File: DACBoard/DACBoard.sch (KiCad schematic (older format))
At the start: 71 parts

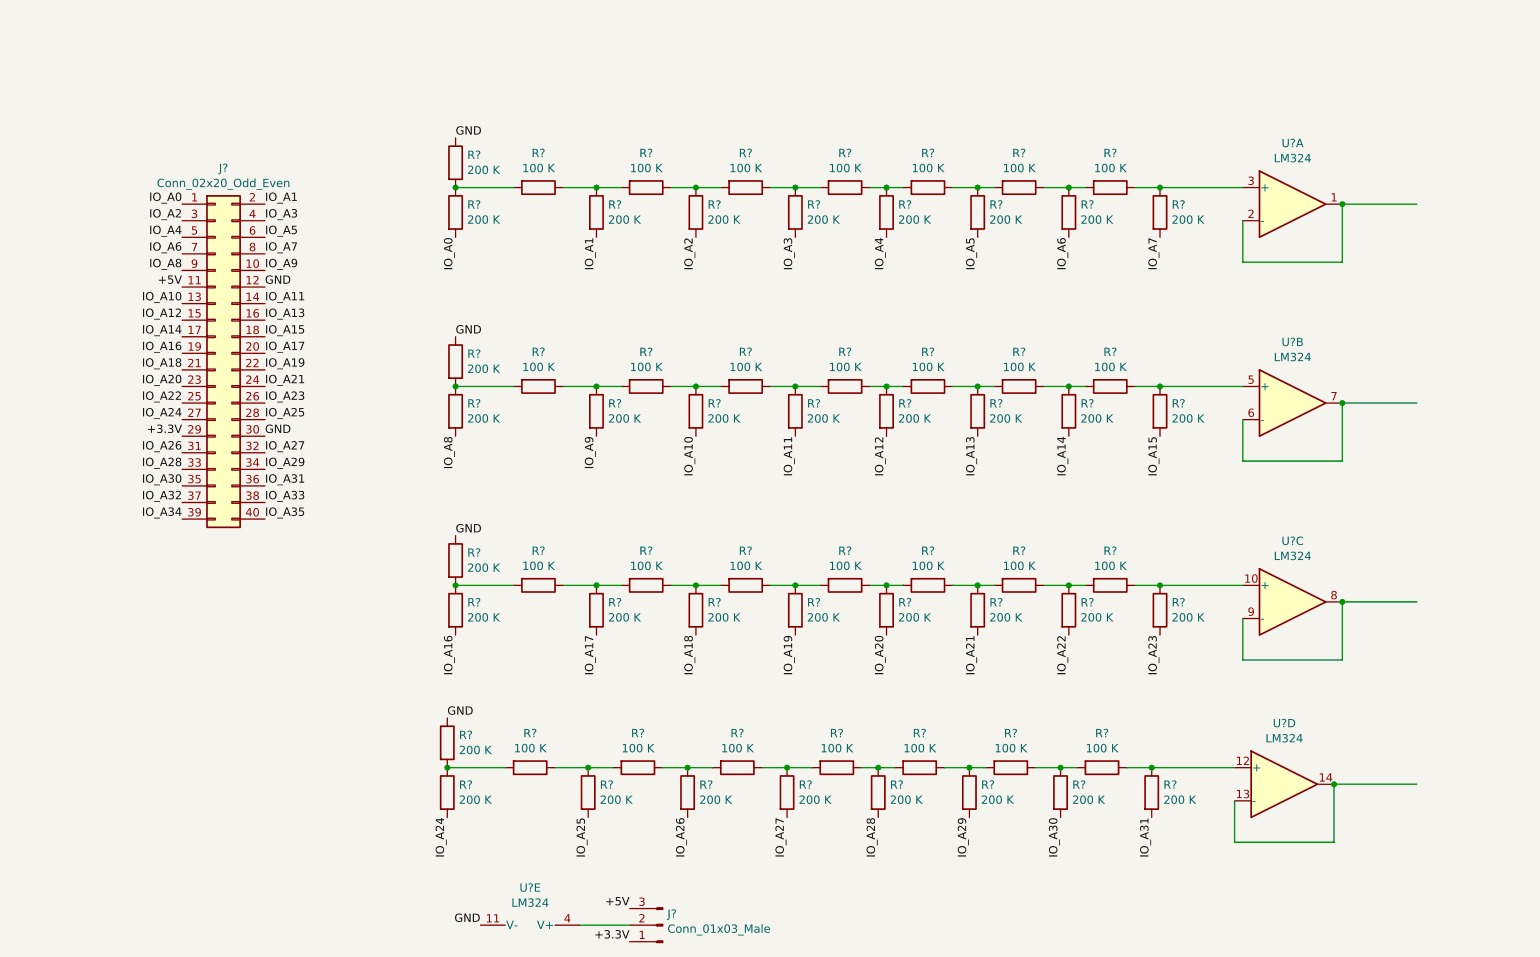
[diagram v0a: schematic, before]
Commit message: Working on DAC PCB, about to make big design changes to it because the layout is impossible.
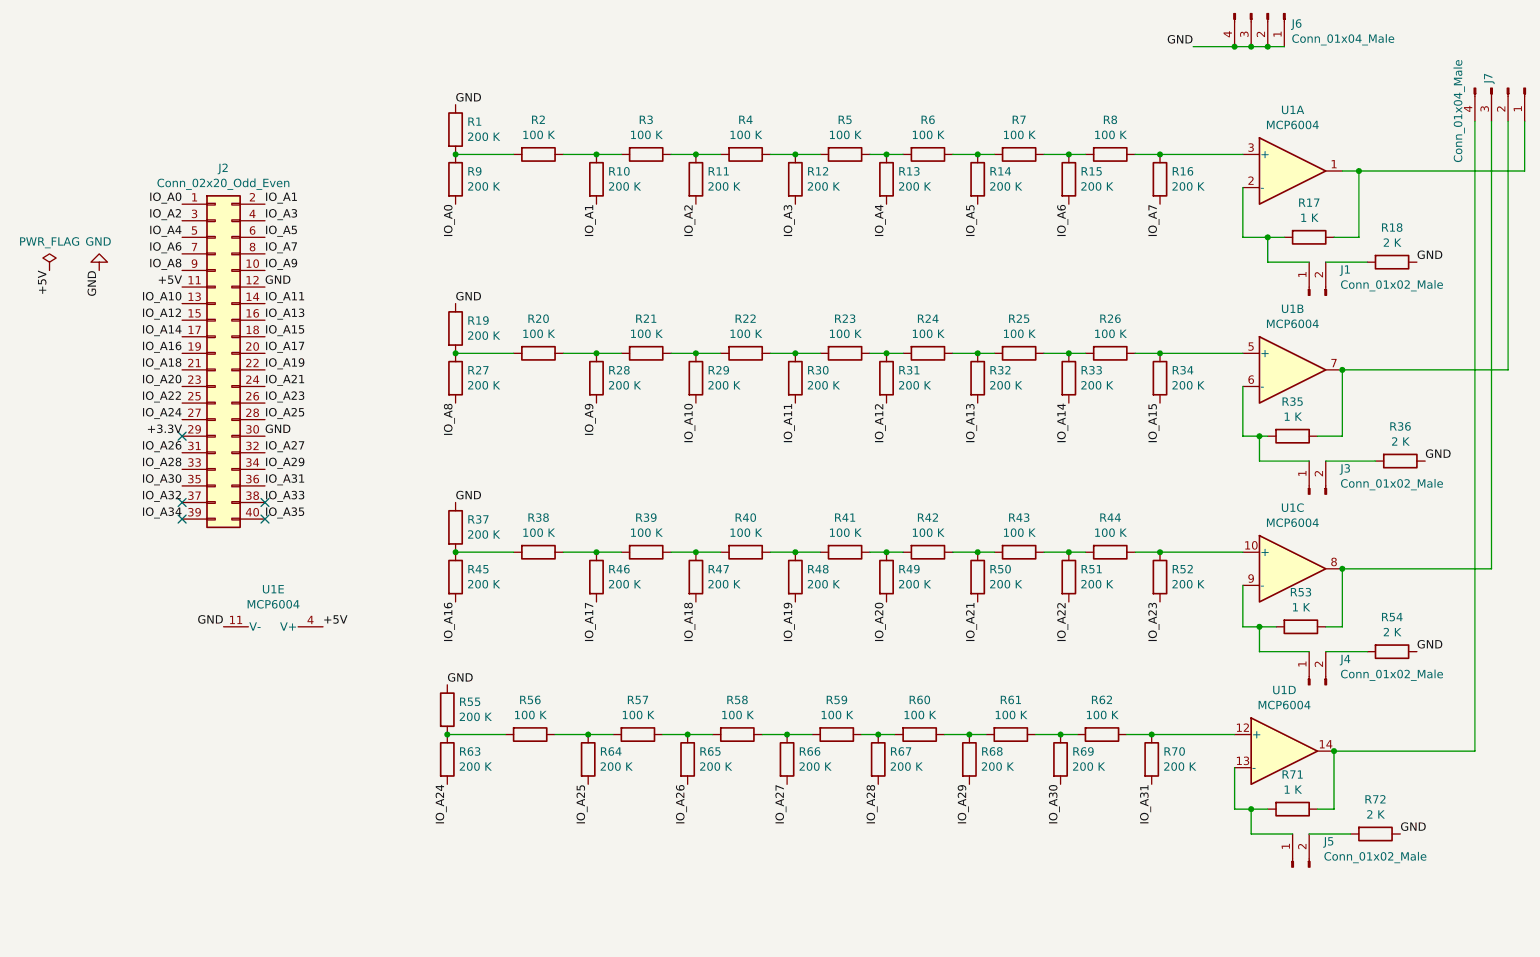
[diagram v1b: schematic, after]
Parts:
- removed J?: Conn_01x03_Male, symbol Connector:Conn_01x03_Male
- removed U? (x5): LM324, symbol Amplifier_Operational:LM324
- added J1, J3, J4, J5: Conn_01x02_Male, Connector_PinHeader_2.54mm:PinHeader_1x02_P2.54mm_Vertical, symbol Connector:Conn_01x02_Male
- added J6, J7: Conn_01x04_Male, Connector_PinHeader_2.54mm:PinHeader_1x04_P2.54mm_Vertical, symbol Connector:Conn_01x04_Male
- added R17, R35, R53, R71: 1 K, Resistor_THT:R_Axial_DIN0207_L6.3mm_D2.5mm_P7.62mm_Horizontal, symbol Device:R
- added R18, R36, R54, R72: 2 K, Resistor_THT:R_Axial_DIN0207_L6.3mm_D2.5mm_P7.62mm_Horizontal, symbol Device:R
- added U1: MCP6004, Package_DIP:DIP-14_W7.62mm, symbol Amplifier_Operational:MCP6004
- J2: renamed from J?; footprint (none) -> Connector_PinSocket_2.54mm:PinSocket_2x20_P2.54mm_Vertical
- R1, R10, R11, R12, R13, R14, R15, R16, R19, R2, R20, R21, R22, R23, R24, R25, R26, R27, R28, R29, R3, R30, R31, R32, R33, R34, R37, R38, R39, R4, R40, R41, R42, R43, R44, R45, R46, R47, R48, R49, R5, R50, R51, R52, R55, R56, R57, R58, R59, R6, R60, R61, R62, R63, R64, R65, R66, R67, R68, R69, R7, R70, R8, R9: renamed from R?; footprint (none) -> Resistor_THT:R_Axial_DIN0207_L6.3mm_D2.5mm_P7.62mm_Horizontal
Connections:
- wire segments 77 -> 105
- no-connect marks 0 -> 5
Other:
- moved on the sheet: R1, R10, R11, R12, R13, R14, R15, R16, R19, R2, R20, R21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

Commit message: Finished first version of design.
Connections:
- net IO_A1: now also R27.2; no longer R10.2
- net IO_A10: now also R14.2; no longer R29.2
- net IO_A11: now also R32.2; no longer R30.2
- net IO_A12: now also R15.2; no longer R31.2
- net IO_A13: now also R33.2; no longer R32.2
- net IO_A14: now also R16.2; no longer R33.2
- net IO_A17: now also R63.2; no longer R46.2
- net IO_A18: now also R46.2; no longer R47.2
- net IO_A19: now also R64.2; no longer R48.2
- net IO_A2: now also R10.2; no longer R11.2
- net IO_A20: now also R47.2; no longer R49.2
- net IO_A21: now also R65.2; no longer R50.2
- net IO_A22: now also R48.2; no longer R51.2
- net IO_A23: now also R66.2; no longer R52.2
- net IO_A24: now also R49.2; no longer R63.2
- net IO_A25: now also R67.2; no longer R64.2
- net IO_A26: now also R50.2; no longer R65.2
- net IO_A27: now also R68.2; no longer R66.2
- net IO_A28: now also R51.2; no longer R67.2
- net IO_A29: now also R69.2; no longer R68.2
- net IO_A3: now also R28.2; no longer R12.2
- net IO_A30: now also R52.2; no longer R69.2
- net IO_A4: now also R11.2; no longer R13.2
- net IO_A5: now also R29.2; no longer R14.2
- net IO_A6: now also R12.2; no longer R15.2
- net IO_A7: now also R30.2; no longer R16.2
- net IO_A8: now also R13.2; no longer R27.2
- net IO_A9: now also R31.2; no longer R28.2
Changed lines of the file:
@@
 $EndComp
 Text Label 5450 2450 3    50   ~ 0
-IO_A1
+IO_A2
 $Comp
 L Device:R R11
@@
 $EndComp
 Text Label 6050 2450 3    50   ~ 0
-IO_A2
+IO_A4
 Text Label 6650 2450 3    50   ~ 0
-IO_A3
+IO_A6
 Text Label 7200 2450 3    50   ~ 0
-IO_A4
+IO_A8
 Text Label 7750 2450 3    50   ~ 0
-IO_A5
+IO_A10
 Text Label 8300 2450 3    50   ~ 0
-IO_A6
+IO_A12
 Text Label 8850 2450 3    50   ~ 0
-IO_A7
+IO_A14
 $Comp
 L Device:R R3
@@
 GND
 Text Label 4600 3650 3    50   ~ 0
-IO_A8
+IO_A1
 $Comp
 L Device:R R20
@@
 $EndComp
 Text Label 5450 3650 3    50   ~ 0
-IO_A9
+IO_A3
 $Comp
 L Device:R R29
@@
 $EndComp
 Text Label 6050 3650 3    50   ~ 0
-IO_A10
+IO_A5
 Text Label 6650 3650 3    50   ~ 0
+IO_A7
+Text Label 7200 3650 3    50   ~ 0
+IO_A9
+Text Label 7750 3650 3    50   ~ 0
 IO_A11
-Text Label 7200 3650 3    50   ~ 0
-IO_A12
-Text Label 7750 3650 3    50   ~ 0
+Text Label 8300 3650 3    50   ~ 0
 IO_A13
-Text Label 8300 3650 3    50   ~ 0
-IO_A14
 Text Label 8850 3650 3    50   ~ 0
 IO_A15
@@
 $EndComp
 Text Label 5450 4850 3    50   ~ 0
-IO_A17
+IO_A18
 $Comp
 L Device:R R47
@@
 $EndComp
 Text Label 6050 4850 3    50   ~ 0
-IO_A18
+IO_A20
 Text Label 6650 4850 3    50   ~ 0
-IO_A19
+IO_A22
 Text Label 7200 4850 3    50   ~ 0
-IO_A20
+IO_A24
 Text Label 7750 4850 3    50   ~ 0
-IO_A21
+IO_A26
 Text Label 8300 4850 3    50   ~ 0
-IO_A22
+IO_A28
 Text Label 8850 4850 3    50   ~ 0
-IO_A23
+IO_A30
 $Comp
 L Device:R R39
@@
 GND
 Text Label 4550 5950 3    50   ~ 0
-IO_A24
+IO_A17
 $Comp
 L Device:R R56
@@
 $EndComp
 Text Label 5400 5950 3    50   ~ 0
-IO_A25
+IO_A19
 $Comp
 L Device:R R65
@@
 $EndComp
 Text Label 6000 5950 3    50   ~ 0
-IO_A26
+IO_A21
 Text Label 6600 5950 3    50   ~ 0
+IO_A23
+Text Label 7150 5950 3    50   ~ 0
+IO_A25
+Text Label 7700 5950 3    50   ~ 0
 IO_A27
-Text Label 7150 5950 3    50   ~ 0
-IO_A28
-Text Label 7700 5950 3    50   ~ 0
+Text Label 8250 5950 3    50   ~ 0
 IO_A29
-Text Label 8250 5950 3    50   ~ 0
-IO_A30
 Text Label 8800 5950 3    50   ~ 0
 IO_A31
